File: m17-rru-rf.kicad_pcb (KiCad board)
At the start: 4 copper layers, 240 x 125 mm, 209 parts, among them J1 LMT87LPM, J2 13.8V, J3 N_PAD, J4 DBG_CONN, J5 SWD_CONN, J6 DA15_CONN, J7 N_PAD, Q1 BSS138, Q2 BSS138, Q3 NP100P04PDG, U1 LT1013DIDR, U10 GAT-30+, U11 CC1200, U12 AD8318, U13 AD8318, U14 STM32F405RGT6, U15 WH3538X-1, U2 LM317_SOT-223, U3 TL431, U4 RA60H3847H1, U5 TP6841, U6 TP6841, U7 CC1200, U8 GAT-30+, U9 SYBD-30-62HP+, X1 40MHz, Y1 12MHz

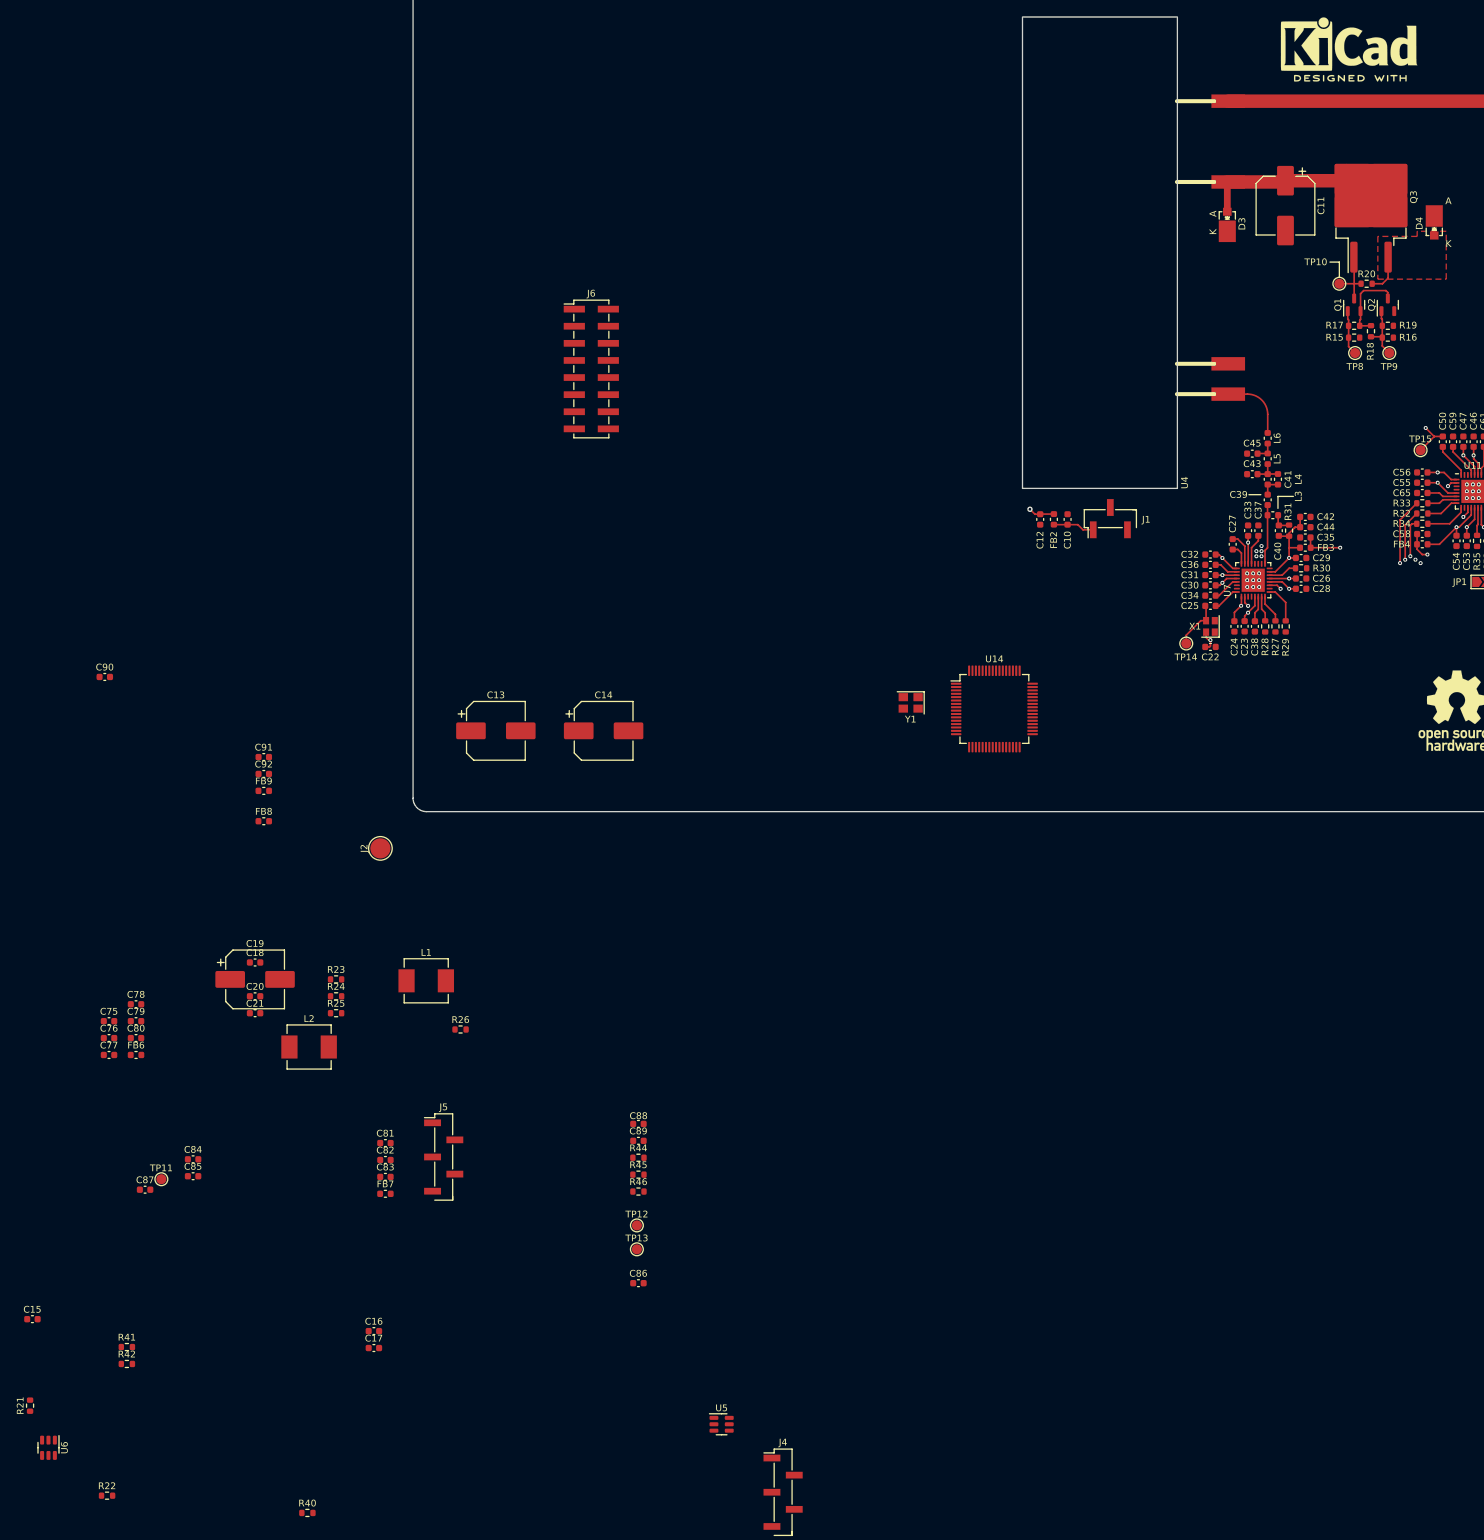
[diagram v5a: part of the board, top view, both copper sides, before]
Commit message: pcb update - PSU
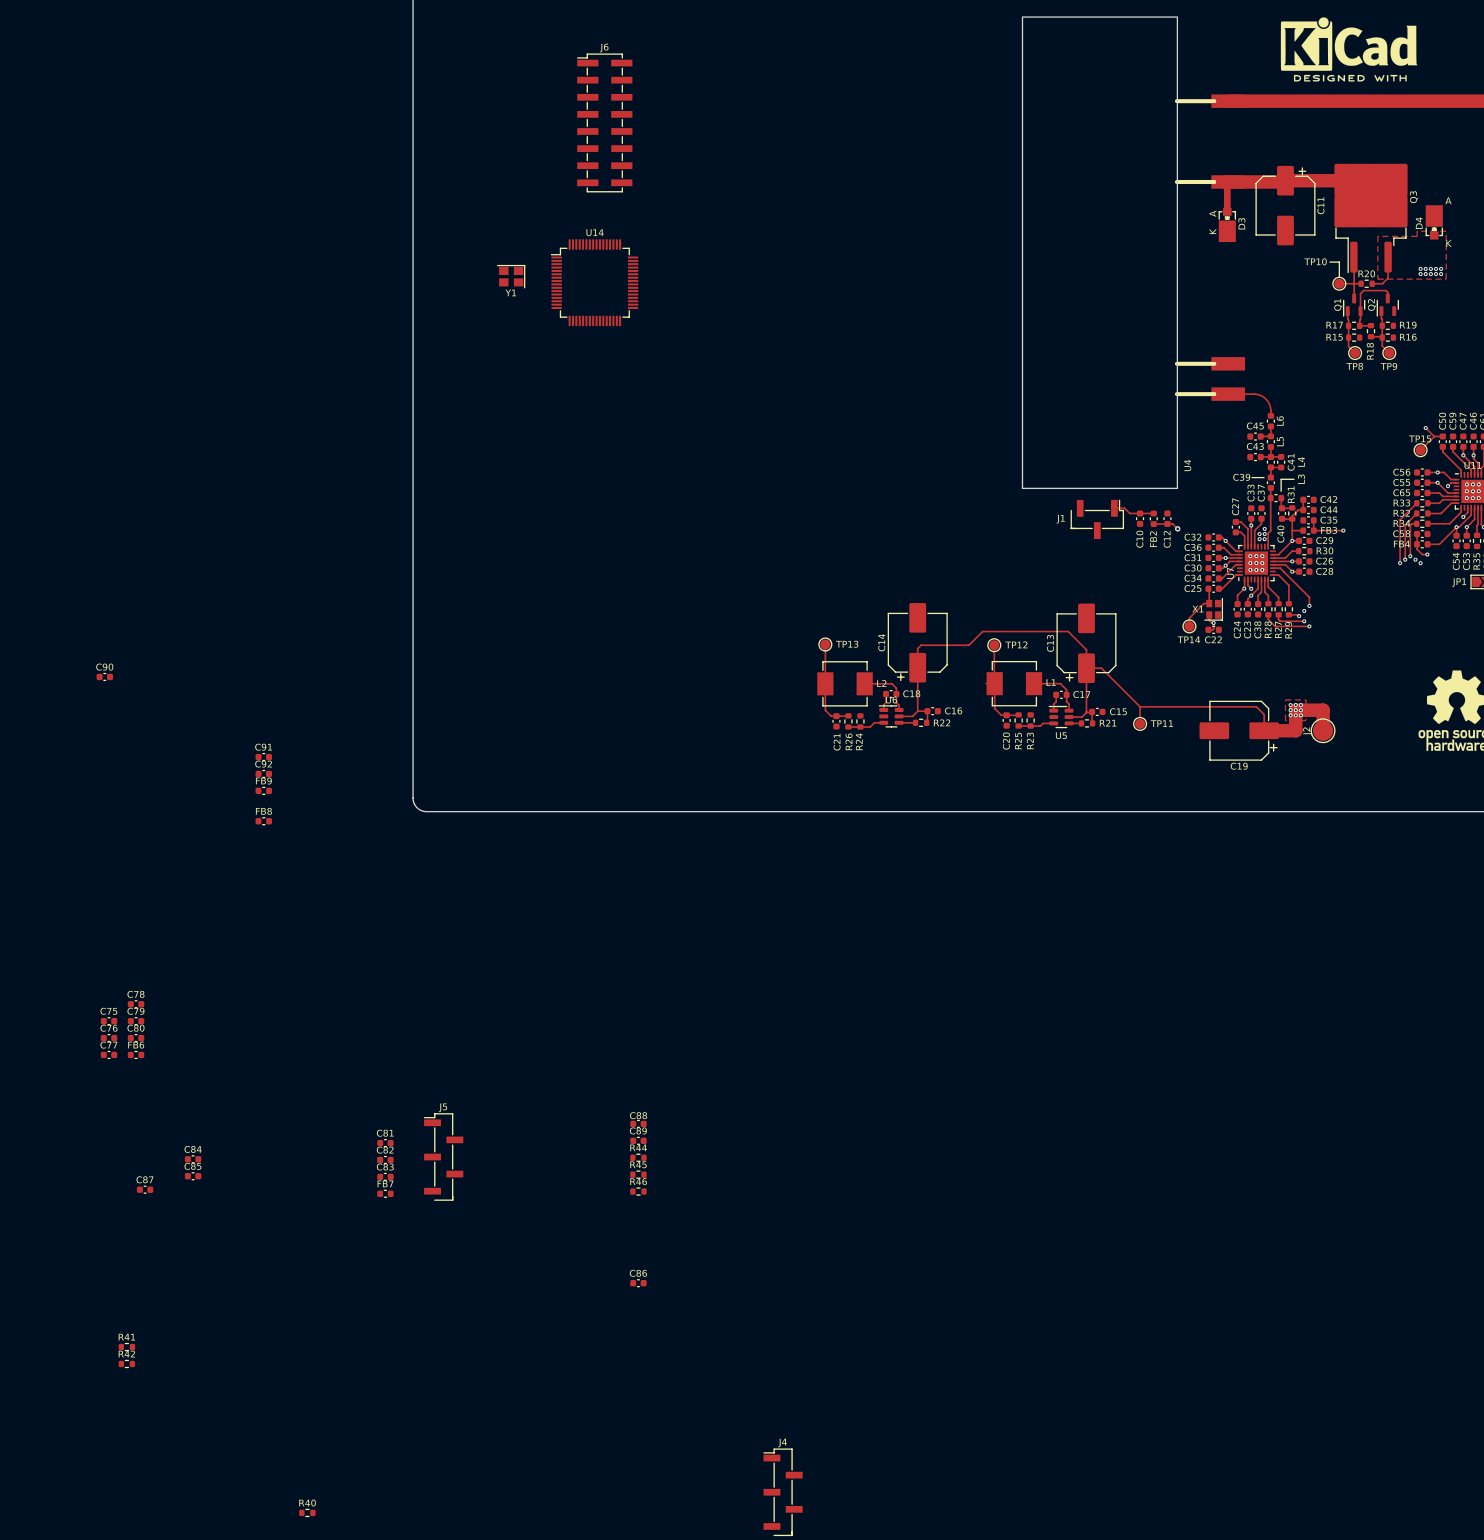
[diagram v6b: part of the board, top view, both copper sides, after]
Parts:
- moved R21 186.8 mm to (180.1, 156.9), turned to 180 degrees
- moved C15 182.0 mm to (181.6, 155.2)
- moved R22 166.7 mm to (155.4, 156.8), turned to 180 degrees
- moved U6 165.7 mm to (151.0, 155.9), turned to 0 degrees
- moved TP11 160.3 mm to (188.0, 157.0)
- moved C19 150.7 mm to (202.7, 158.0), turned to 180 degrees
- moved J2 141.1 mm to (215.1, 158.0)
- moved C17 140.8 mm to (176.3, 152.7)
- moved C16 123.9 mm to (157.2, 155.1)
- moved C20 118.9 mm to (168.1, 156.5), turned to 90 degrees
- moved U5 116.5 mm to (176.3, 155.9)
- moved R25 110.3 mm to (169.9, 156.5), turned to 90 degrees
- moved R23 110.1 mm to (171.7, 156.5), turned to 90 degrees
- moved C18 102.5 mm to (151.0, 152.5)
- moved TP12 101.2 mm to (166.3, 145.3)
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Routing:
- net /Power supply/13.8V_OUT: track 19.7 -> 209.9 mm, vias 1 -> 20
- net /Power supply/5V_OUT: track 3.30 -> 16.9 mm
- net /Exciter/3.3V_IN: track 13.9 -> 27.4 mm
- net /nRST: track 16.0 -> 25.2 mm, vias 3 -> 4
- net Net-(U5-SW): track 0.00 -> 8.46 mm
- net Net-(U6-SW): track 0.00 -> 8.39 mm
- net /SPI_MOSI: track 9.92 -> 17.1 mm, vias 1 -> 2
- net /TX_nCS: track 1.84 -> 8.50 mm
- net Net-(U6-FB): track 0.00 -> 5.51 mm
- net Net-(U5-FB): track 0.00 -> 5.37 mm
- net /SPI_SCK: track 7.57 -> 12.2 mm, vias 1 -> 2
- net Net-(U6-BST): track 0.00 -> 2.50 mm
- net Net-(U5-BST): track 0.00 -> 2.50 mm
- net Net-(U6-EN): track 0.00 -> 2.45 mm
- net Net-(U5-EN): track 0.00 -> 1.85 mm
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- added copper zone on In1.Cu, net /Power supply/13.8V_OUT

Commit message: pcb update
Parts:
- removed REF**: KiCad-Logo2_8mm_SilkScreen, Symbol:KiCad-Logo2_8mm_SilkScreen
- removed REF**: OSHW-Logo_11.4x12mm_SilkScreen, Symbol:OSHW-Logo_11.4x12mm_SilkScreen
- added FID1: Fiducial, Fiducial:Fiducial_0.75mm_Mask1.5mm, F.Cu at (129.0, 159.0)
- added FID2: Fiducial, Fiducial:Fiducial_0.75mm_Mask1.5mm, F.Cu at (158.0, 54.0)
- added FID3: Fiducial, Fiducial:Fiducial_0.75mm_Mask1.5mm, F.Cu at (311.0, 135.0)
- added H1: 3.2mm, MountingHole:MountingHole_3.2mm_M3_Pad_Via, F.Cu at (123.0, 50.0)
- added H10: 3.2mm, MountingHole:MountingHole_3.2mm_M3_Pad_Via, F.Cu at (277.5, 107.5)
- added H11: 3.2mm, MountingHole:MountingHole_3.2mm_M3_Pad_Via, F.Cu at (316.0, 107.5)
- added H12: 3.2mm, MountingHole:MountingHole_3.2mm_M3_Pad_Via, F.Cu at (264.5, 142.5)
- added H13: 3.2mm, MountingHole:MountingHole_3.2mm_M3_Pad_Via, F.Cu at (189.5, 148.5)
- added H14: 3.2mm, MountingHole:MountingHole_3.2mm_M3_Pad_Via, F.Cu at (222.5, 165.0)
- added H2: 3.2mm, MountingHole:MountingHole_3.2mm_M3_Pad_Via, F.Cu at (315.0, 50.0)
- added H3: 3.2mm, MountingHole:MountingHole_3.2mm_M3_Pad_Via, F.Cu at (315.0, 165.0)
- added H4: 3.2mm, MountingHole:MountingHole_3.2mm_M3_Pad_Via, F.Cu at (123.0, 165.0)
- added H5: 3.2mm, MountingHole:MountingHole_3.2mm_M3_Pad_Via, F.Cu at (166.5, 50.0)
- added H6: 3.2mm, MountingHole:MountingHole_3.2mm_M3_Pad_Via, F.Cu at (242.5, 50.0)
- added H7: 3.2mm, MountingHole:MountingHole_3.2mm_M3_Pad_Via, F.Cu at (166.5, 134.5)
- added H8: 3.2mm, MountingHole:MountingHole_3.2mm_M3_Pad_Via, F.Cu at (215.5, 107.5)
- added H9: 3.2mm, MountingHole:MountingHole_3.2mm_M3_Pad_Via, F.Cu at (252.5, 107.5)
- moved R40 192.0 mm to (143.7, 99.3), turned to 90 degrees
- moved R42 184.3 mm to (140.7, 99.3), turned to 90 degrees
- moved R41 183.1 mm to (142.2, 99.3), turned to 90 degrees
- moved C87 165.1 mm to (153.1, 105.6)
- moved R44 163.2 mm to (145.0, 61.3)
- moved R45 163.2 mm to (145.0, 63.8)
- moved R46 163.2 mm to (145.0, 66.3)
- moved C84 151.2 mm to (153.1, 113.5)
- moved C90 150.0 mm to (154.7, 60.7)
- moved J4 149.0 mm to (149.5, 122.8), turned to 90 degrees
- moved C80 148.4 mm to (153.1, 108.9), turned to 180 degrees
- moved C77 148.3 mm to (153.1, 116.6)
- moved C78 146.2 mm to (153.1, 107.3)
- moved J5 142.5 mm to (151.9, 95.7)
- moved FB7 139.6 mm to (153.1, 110.5), turned to 180 degrees
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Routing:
- net /MCU/MCU_3V3: track 0.00 -> 70.3 mm, vias 0 -> 5
- net /nRST: track 25.2 -> 50.1 mm, vias 4 -> 6
- net /MCU/SWDIO: track 0.00 -> 16.3 mm, vias 0 -> 2
- net /MCU/DBG_TX: track 0.00 -> 12.4 mm
- net /MCU/SWDCLK: track 0.00 -> 12.0 mm
- net /MCU/DBG_RX: track 0.00 -> 10.7 mm
- net /MCU/OSC1: track 0.00 -> 10.4 mm
- net /MCU/MCU_VDDA_3V3: track 0.00 -> 9.46 mm
- net Net-(U14-VCAP_1): track 0.00 -> 9.35 mm
- net /MCU/TP1: track 0.00 -> 8.78 mm
- net /MCU/OSC2: track 0.00 -> 8.25 mm
- net /MCU/TP2: track 0.00 -> 7.81 mm
- net /Exciter/3.3V_IN: track 27.4 -> 34.8 mm, vias 3 -> 4
- net Net-(U14-PA2): track 0.00 -> 5.37 mm
- net Net-(U14-PB5): track 0.00 -> 5.15 mm
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- added copper zone on B.Cu, net GND
- added copper zone on F.Cu, net GND
- added copper zone on In1.Cu, net GND
- added copper zone on In2.Cu, net GND
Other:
- board size 240 x 125 mm -> 202 x 125 mm
- board text added: "DRX"
- board text added: "DTX"
- board text added: "GND"
- board text added: "SWCLK"
- board text added: "SWDIO"
- board text added: "TP1"
- board text added: "TP2"
- board text added: "U_MCU"
- board text added: "nRST"

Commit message: pcb update
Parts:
- moved C90 20.8 mm to (143.3, 78.0), turned to 180 degrees
- moved J6 19.1 mm to (151.9, 69.1)
- moved FB9 13.8 mm to (143.3, 75.4), turned to 180 degrees
- moved C91 13.8 mm to (143.3, 70.4)
- moved C92 13.8 mm to (143.3, 72.9)
- moved H8 3.00 mm to (212.5, 107.5)
- moved R44 2.43 mm to (143.3, 63.0), turned to 180 degrees
- moved R46 2.28 mm to (143.3, 67.8), turned to 180 degrees
- moved R45 2.26 mm to (143.3, 65.3), turned to 180 degrees
- moved FB2 2.05 mm to (190.0, 124.5)
- moved C10 2.04 mm to (188.0, 124.5)
- moved C12 2.04 mm to (192.0, 124.5)
- moved C13 2.03 mm to (178.0, 145.0)
- moved C14 2.03 mm to (152.9, 144.9)
- moved C15 2.03 mm to (179.6, 155.2)
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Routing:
- net /MCU/RF_PWR_SP: track 0.00 -> 170.3 mm, vias 0 -> 2
- net /RF PA/RF_PA_VGG: track 10.4 -> 130.9 mm, vias 1 -> 2
- net /Exciter/3.3V_IN: track 34.8 -> 137.5 mm, vias 4 -> 6
- net /FWD_SENSE: track 18.8 -> 46.6 mm, vias 3 -> 4
- net /nRST: track 50.1 -> 74.5 mm, vias 6 -> 4
- net /SPI_MISO: track 7.23 -> 31.5 mm, vias 2 -> 4
- net /SPI_SCK: track 12.2 -> 34.7 mm, vias 2 -> 3
- net /SPI_MOSI: track 17.1 -> 39.2 mm, vias 2 -> 3
- net /Interface/INTERFACE_3V3: track 0.00 -> 10.2 mm
- net /Receiver/RX_3V3: track 79.7 -> 89.1 mm, vias 9 -> 10
- net /RX_nCS: track 15.3 -> 24.4 mm
- net /Interface/MCU_TX: track 3.35 -> 6.68 mm, vias 1 -> 2
- net /Interface/PA_EN: track 0.00 -> 3.33 mm, vias 0 -> 1
- net /REF_SENSE: track 8.29 -> 11.6 mm, vias 1 -> 2
- net /Interface/TEMP_SENSE: track 0.00 -> 3.30 mm, vias 0 -> 1
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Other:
- board text added: "13.8V"
- board text added: "3.3V"
- board text added: "5.0V"
